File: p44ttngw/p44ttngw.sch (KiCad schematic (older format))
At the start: 67 parts, among them J1 CONN_02X04, J2 HLJ-6115ANL, J3 CONN_02X12, J4 USB_A, J6 USB_Micro_AB, J8 HLJ-6115ANL, P1 FDI_Cable, P3 CONN_02X02, SW1 Omron PB, U1 ONION-OMEGA2S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

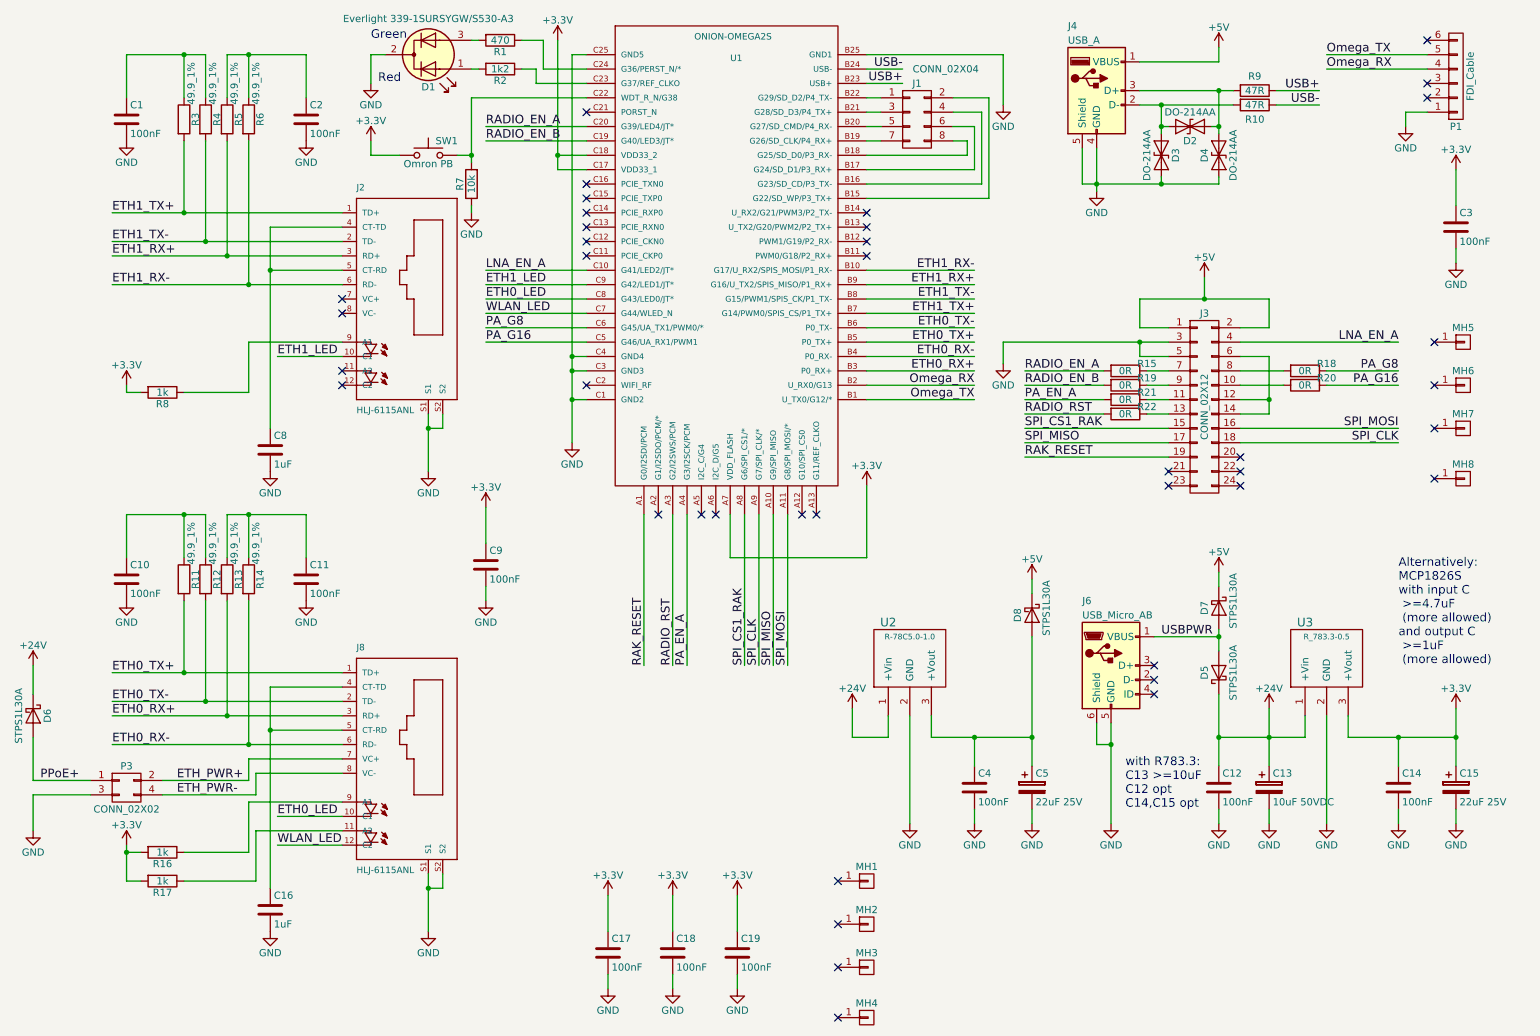
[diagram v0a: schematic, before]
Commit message: Complete PCB for P44-DSB Hammond case, but mechanical check pending
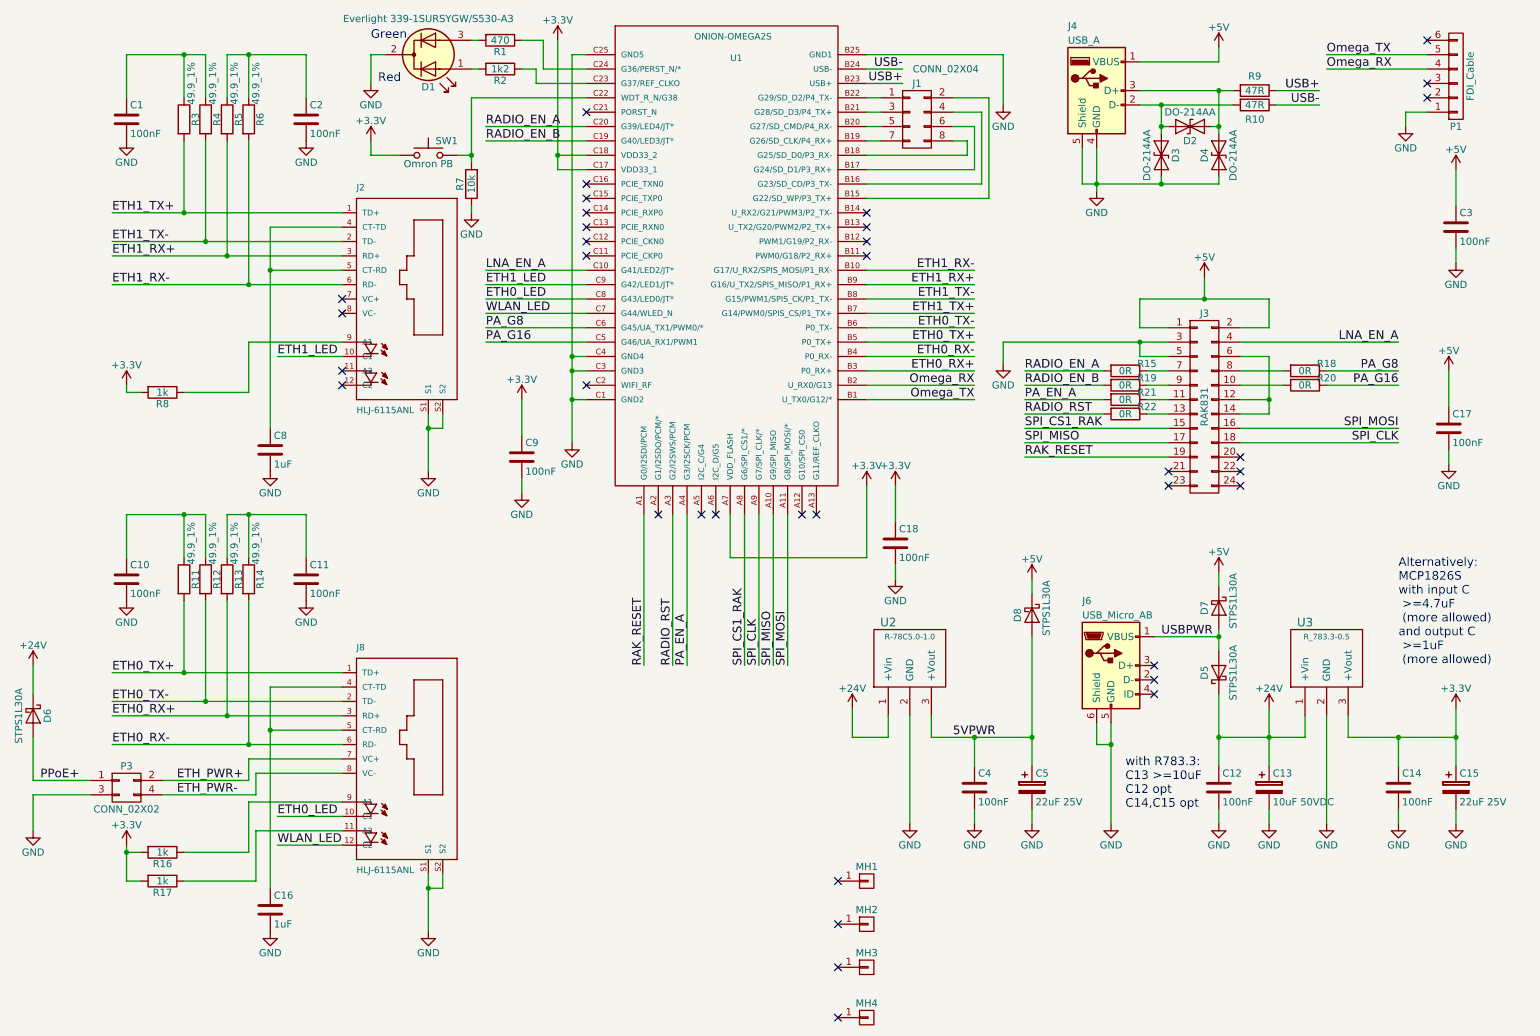
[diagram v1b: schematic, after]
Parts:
- removed C19: 100nF, Capacitors_SMD:C_1206_HandSoldering, symbol C
- removed MH5, MH6, MH7, MH8: CONN_01X01, Mounting_Holes:MountingHole_3.2mm_M3_DIN965_Pad, symbol CONN_01X01
- J3: value CONN_02X12 -> RAK831; footprint Pin_Headers:Pin_Header_Straight_2x12_Pitch2.54mm -> plan44:RAK831
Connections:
- net +3V3: no longer C17.1, C3.1
- net +5V: now also C17.1, C3.1
- net 5VPWR: now reaches C4.1, C5.1, D8.2 (A), U2.3 (+Vout)
- no-connect marks 40 -> 36
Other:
- moved on the sheet: C17, C18, C9

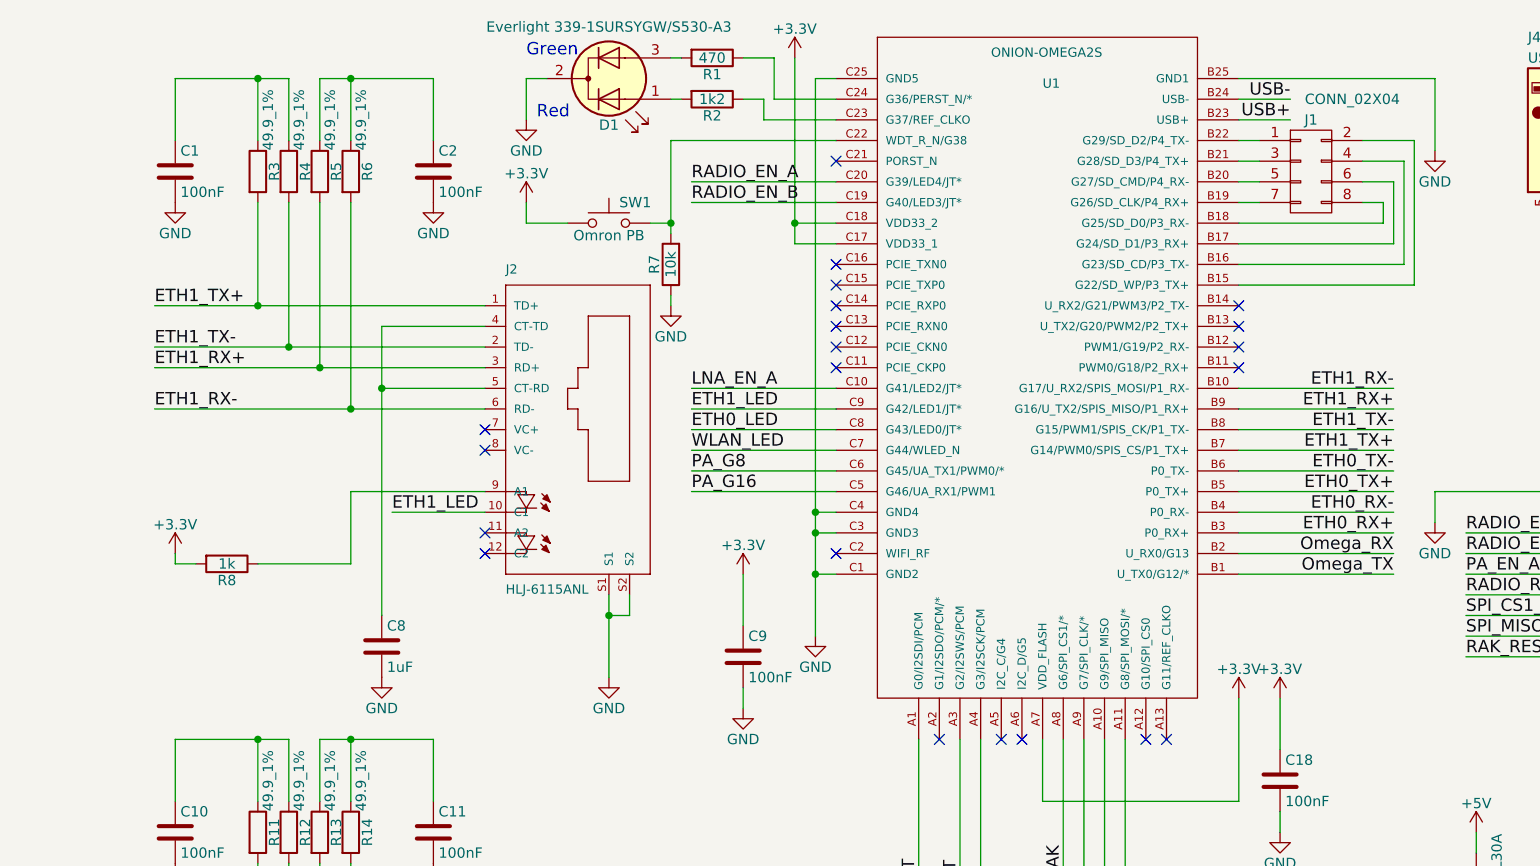
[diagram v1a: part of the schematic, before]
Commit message: Completely redesigned for IP65 Hammond 1554E (90x90x60)
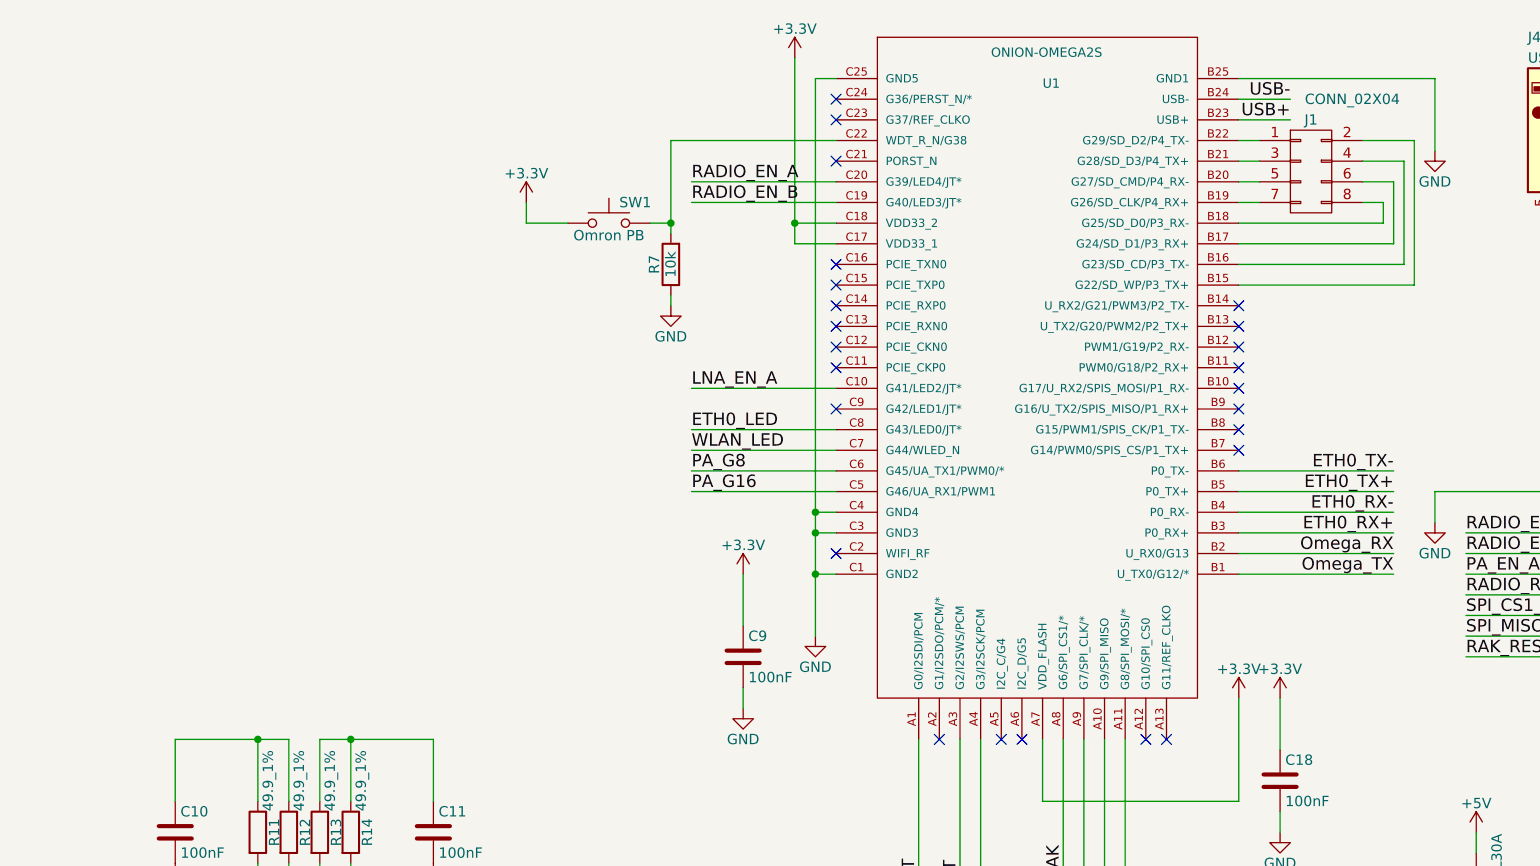
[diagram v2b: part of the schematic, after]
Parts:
- removed C1, C2: 100nF, Capacitors_SMD:C_1206_HandSoldering, symbol C
- removed C8: 1uF, Capacitors_SMD:C_1206_HandSoldering, symbol C
- removed D1: Everlight 339-1SURSYGW/S530-A3, LEDs:LED_D5.0mm-3, symbol LED_Dual_ACA
- removed J2: HLJ-6115ANL, plan44:HLJ-6115ANL, symbol HLJ-6115ANL
- removed R1: 470, Resistors_SMD:R_1206_HandSoldering, symbol R
- removed R2: 1k2, Resistors_SMD:R_1206_HandSoldering, symbol R
- removed R3, R4, R5, R6: 49.9_1%, Resistors_SMD:R_0805_HandSoldering, symbol R
- removed R8: 1k, Resistors_SMD:R_1206_HandSoldering, symbol R
- U2: Field5 169-07-680 -> 110-34-511
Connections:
- net ETH1_LED: no longer names the net of U1.C9 (G42/LED1/JT*)
- net ETH1_RX+: no longer names the net of U1.B9 (G16/U_TX2/SPIS_MISO/P1_RX+)
- net ETH1_RX-: no longer names the net of U1.B10 (G17/U_RX2/SPIS_MOSI/P1_RX-)
- net ETH1_TX+: no longer names the net of U1.B7 (G14/PWM0/SPIS_CS/P1_TX+)
- net ETH1_TX-: no longer names the net of U1.B8 (G15/PWM1/SPIS_CK/P1_TX-)
- no-connect marks 36 -> 39
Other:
- note removed: "Green"
- note removed: "Red"

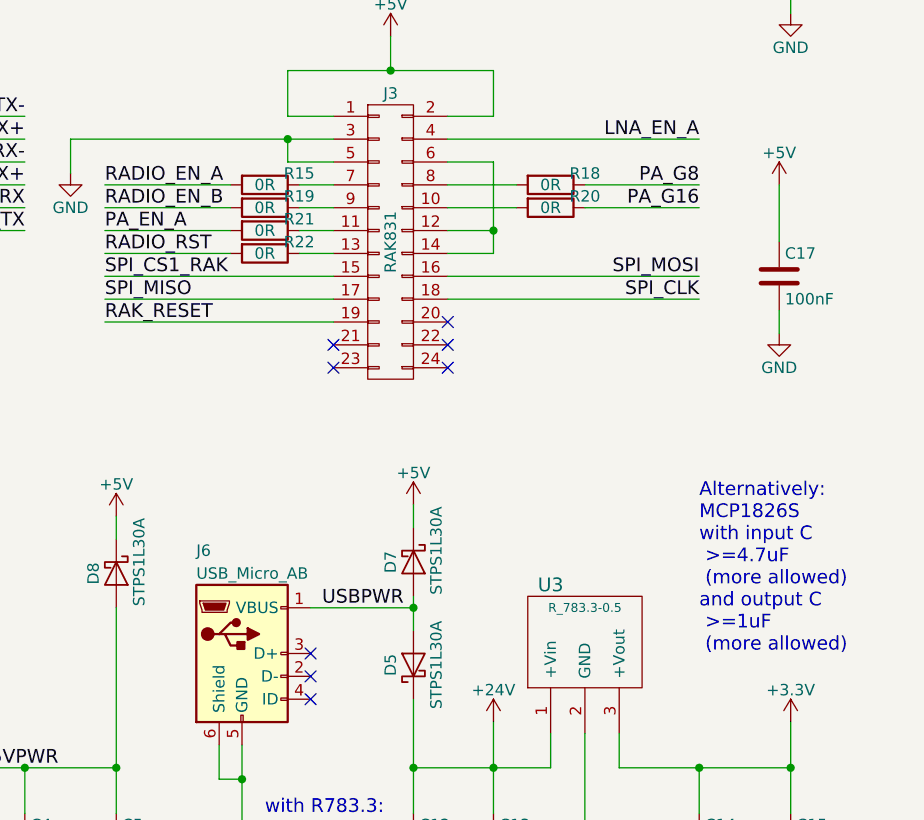
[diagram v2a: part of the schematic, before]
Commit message: RAK831 pins 6,12 and 14 were connected together, but not to GND as they should. Fixed manually in layout, track width between 6 and 12 is narrow, no room for power net (and not needed).
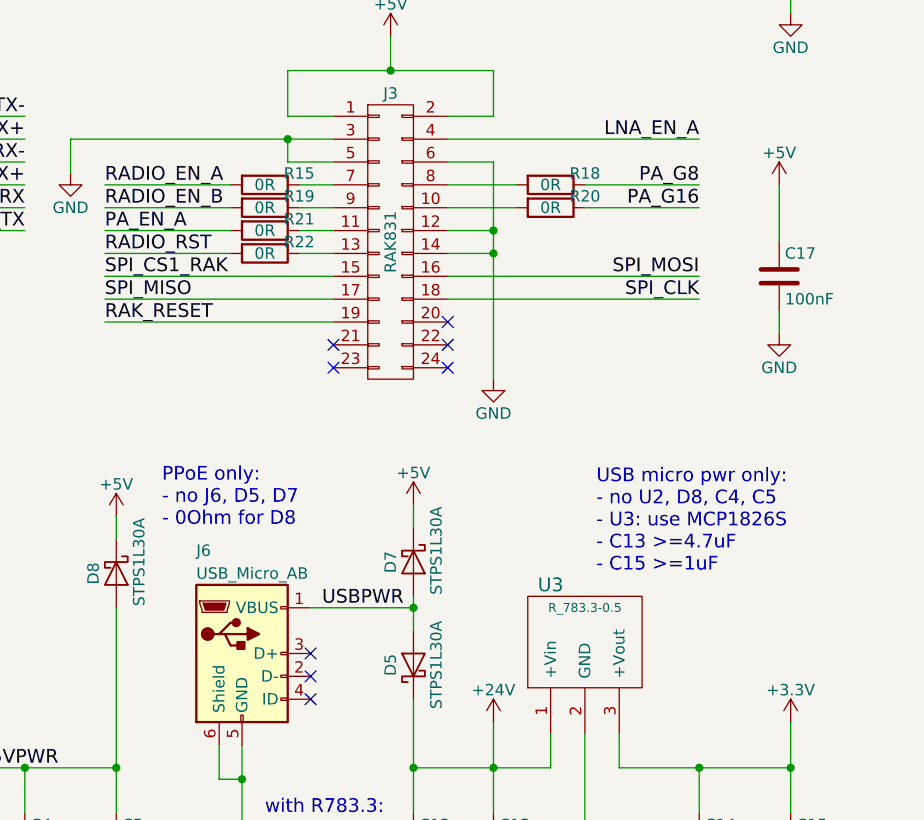
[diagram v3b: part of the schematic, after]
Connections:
- net GND: now also J3.12 (P12), J3.14 (P14), J3.6 (P6)
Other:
- note added: "PPoE only:\n- no J6, D5, D7\n- 0Ohm for D8"
- note added: "USB micro pwr only:\n- no U2, D8, C4, C5\n- U3: use MCP1826S\n- C13 >=4.7uF\n- C15 >=1uF"
- note removed: "Alternatively:\nMCP1826S\nwith input C\n >=4.7uF\n (more allowed)\nand output C\n >=1uF\n (more allowed)"
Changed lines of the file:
@@
 	9500 5400 9500 5800
 Connection ~ 9500 5600
-Text Notes 10400 5100 0    60   ~ 0
-Alternatively:\nMCP1826S\nwith input C\n >=4.7uF\n (more allowed)\nand output C\n >=1uF\n (more allowed)
+Text Notes 9950 4750 0    60   ~ 0
+USB micro pwr only:\n- no U2, D8, C4, C5\n- U3: use MCP1826S\n- C13 >=4.7uF\n- C15 >=1uF
 Text Notes 8500 6100 0    60   ~ 0
 with R783.3:\nC13 >=10uF\nC12 opt\nC14,C15 opt
@@
 	9300 2950 9500 2950
 Wire Wire Line
-	9500 2950 9500 3350
+	9500 2950 9500 3900
 Wire Wire Line
 	9500 3250 9300 3250
@@
 NoConn ~ 4750 950
 NoConn ~ 4750 1050
+$Comp
+L GND #PWR?
+U 1 1 5A147972
+P 9500 3900
+F 0 "#PWR?" H 9500 3650 50  0001 C CNN
+F 1 "GND" H 9500 3750 50  0000 C CNN
+F 2 "" H 9500 3900 50  0000 C CNN
+F 3 "" H 9500 3900 50  0000 C CNN
+	1    9500 3900
+	1    0    0    -1
+$EndComp
+Connection ~ 9500 3350
+Text Notes 8050 4550 0    60   ~ 0
+PPoE only:\n- no J6, D5, D7\n- 0Ohm for D8
 $EndSCHEMATC
